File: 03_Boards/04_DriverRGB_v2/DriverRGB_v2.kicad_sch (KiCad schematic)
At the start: 22 parts, among them J1 PJ-102A, J2 S4B-ZR-SM4A, J3 20021121-00006C1LF, Q1 FDD8880, Q2 FDD8880, Q3 FDD8880, U1 ESP-12S, U3 AMS1117CD-3.3

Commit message: PCB
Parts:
- added R9: 10kOhm, Resistor_SMD:R_0603_1608Metric, symbol Device:R
- C3, C4: value 100nF -> 1nF
- S1: value Enable -> Reset
- S2: value IO0 -> Boot
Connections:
- net EN: now also R9.2, S1.2; no longer R9.1, S1.1
- net GND: now also S1.1; no longer R9.2
- net IO0: now also R9.2
- net VDD: now also R9.1, R9.1; no longer S1.2
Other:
- note added: "SWITCH BUTTON"
- moved on the sheet: C3, C4, J3, Q1, R2, R3, R9, S1, S2, U1

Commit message: Memoria
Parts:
- removed C4: 1nF, Capacitor_SMD:C_0603_1608Metric, symbol Device:C
- added R9 (x3): 10kOhm, Resistor_SMD:R_0603_1608Metric, symbol Device:R
- C3: value 1nF -> 100nF
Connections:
- net EN: no longer U1.3 (EN)
- net GND: now also R9.1
- net PWM_RED: now also U1.5 (IO14); no longer U1.4 (IO16)
- net VDD: now also R9.1, R9.2
- net RST: now reaches U1.1 (RST)
- net at U1.10 (IO15): now also R9.2
- net at U1.11 (IO2): now also R9.1
- new net: R9.2, U1.3 (EN)
- no-connect marks 8 -> 5

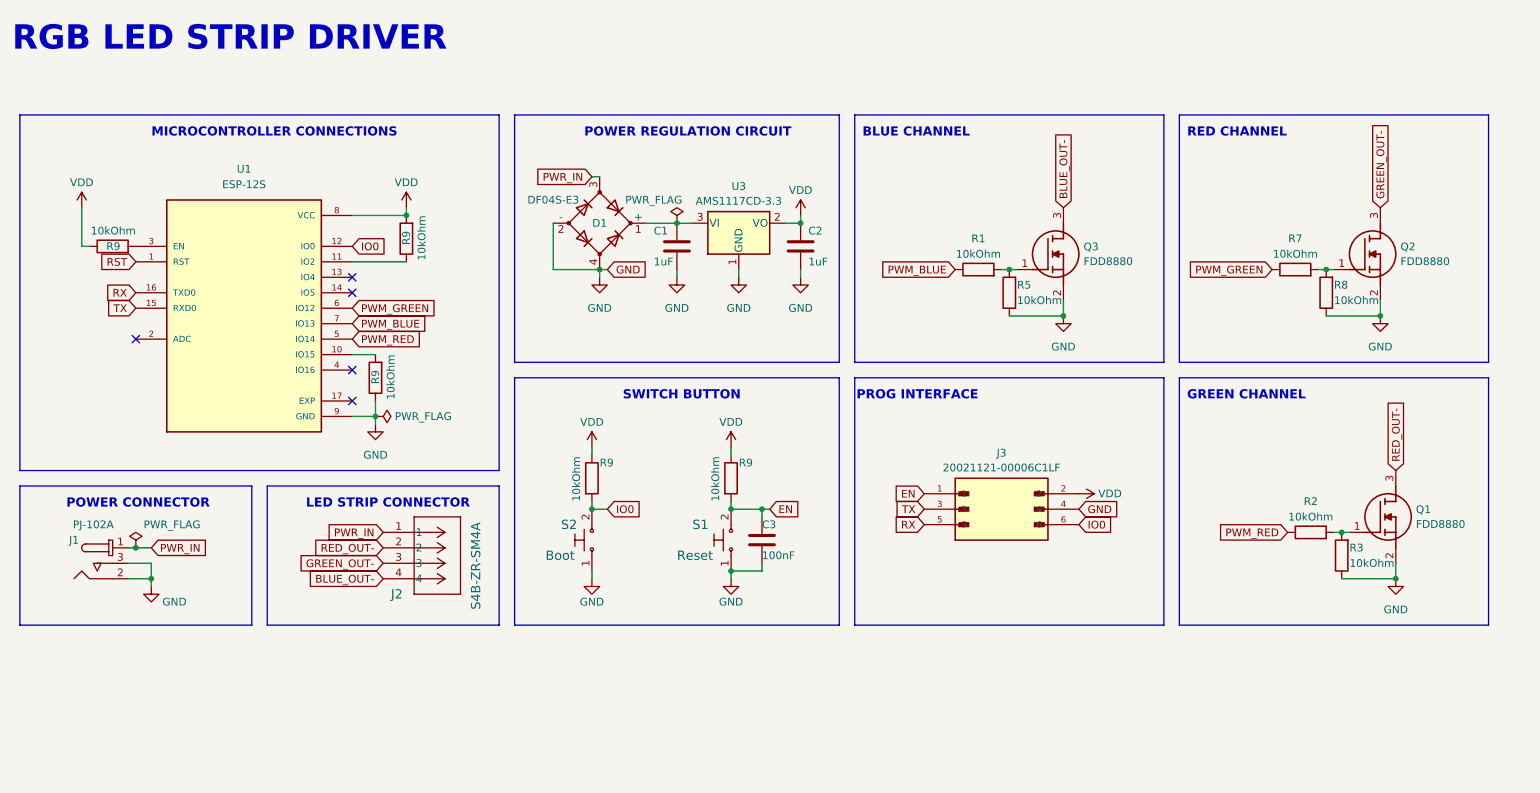
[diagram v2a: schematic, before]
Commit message: Rediseño del esquemático del PCB
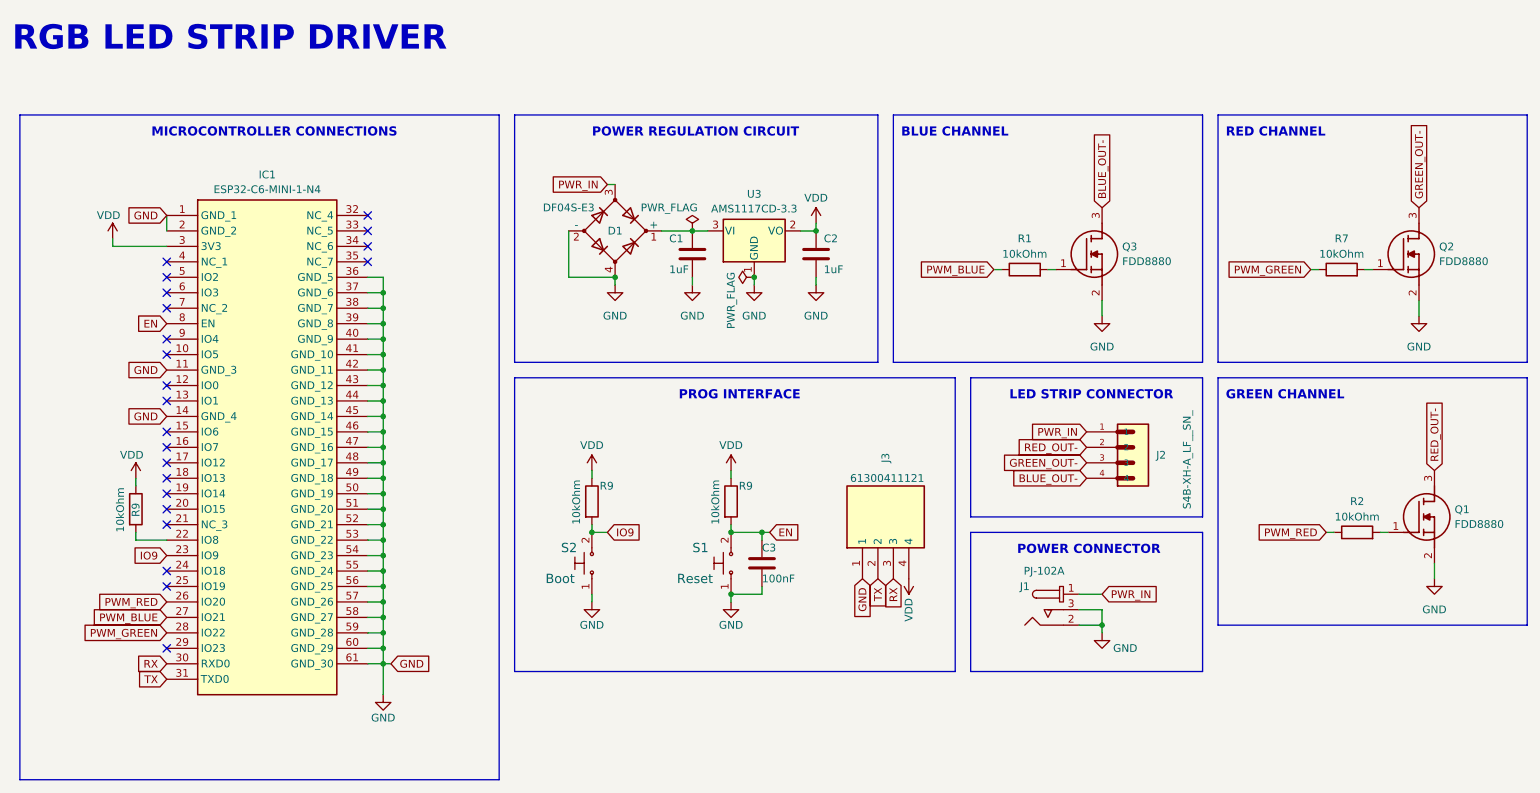
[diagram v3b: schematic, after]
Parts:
- removed J2: S4B-ZR-SM4A, 01_Footprints:S4B-ZR-SM4A-TF-LF, symbol S4B-ZR-SM4A-TF-LF:S4B-ZR-SM4A-TFLFSN
- removed J3: 20021121-00006C1LF, 01_Footprints:20021121-00006C1LF, symbol 20021121-00006C1LF:20021121-00006C1LF
- removed R3, R5, R8, R9 (x3): 10kOhm, Resistor_SMD:R_0603_1608Metric, symbol Device:R
- removed U1: ESP-12S, 01_Footprints:ESP-12S, symbol ESP-12S:ESP-12S
- added IC1: ESP32-C6-MINI-1-N4, 01_Footprints:ESP32-C6-MINI-1-N4, symbol ESP32-C6-MINI-1-N4:ESP32-C6-MINI-1-N4
- added J2: S4B-XH-A_LF__SN_, 01_Footprints:S4B-XH-A_LF__SN_, symbol S4B-XH-A_LF__SN_:S4B-XH-A_LF__SN_
- added J3: 61300411121, 01_Footprints:61300411121, symbol 61300411121:61300411121
- added R9: 10kOhm, Resistor_SMD:R_0603_1608Metric, symbol Device:R
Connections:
- net BLUE_OUT-: now also J2.4
- net EN: now also IC1.8 (EN)
- net GND: now also IC1.1 (GND_1), IC1.11 (GND_3), IC1.14 (GND_4), IC1.2 (GND_2), IC1.36 (GND_5), IC1.37 (GND_6), IC1.38 (GND_7), IC1.39 (GND_8), IC1.40 (GND_9), IC1.41 (GND_10), IC1.42 (GND_11), IC1.43 (GND_12), IC1.44 (GND_13), IC1.45 (GND_14), IC1.46 (GND_15), IC1.47 (GND_16), IC1.48 (GND_17), IC1.49 (GND_18), IC1.50 (GND_19), IC1.51 (GND_20), IC1.52 (GND_21), IC1.53 (GND_22), IC1.54 (GND_23), IC1.55 (GND_24), IC1.56 (GND_25), IC1.57 (GND_26), IC1.58 (GND_27), IC1.59 (GND_28), IC1.60 (GND_29), IC1.61 (GND_30), J3.1
- net GREEN_OUT-: now also J2.3
- net PWM_BLUE: now also IC1.27 (IO21)
- net PWM_GREEN: now also IC1.28 (IO22)
- net PWM_RED: now also IC1.26 (IO20)
- net PWR_IN: now also J2.1
- net RED_OUT-: now also J2.2
- net RX: now also IC1.30 (RXD0), J3.3
- net TX: now also IC1.31 (TXD0), J3.2
- net VDD: now also IC1.3 (3V3), J3.4, R9.1
- net IO0 renamed IO9
- net IO9: now also IC1.23 (IO9)
- new net: IC1.22 (IO8), R9.2
- no-connect marks 5 -> 22
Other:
- note removed: "SWITCH BUTTON"
- moved on the sheet: C1, C2, C3, D1, J1, Q1, Q2, Q3, R1, R2, R7, R9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

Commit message: Board desing v2
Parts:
- renumbered U3 to U1
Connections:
- net PWM_BLUE: now also IC1.26 (IO20); no longer IC1.27 (IO21)
- net PWM_GREEN: now also IC1.27 (IO21); no longer IC1.28 (IO22)
- net PWM_RED: now also IC1.28 (IO22); no longer IC1.26 (IO20)
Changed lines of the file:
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@@
   (title_block
     (title "RGB LED STRIP DRIVER")
-    (date "18/06/2024")
+    (date "20/06/2024")
     (rev "v02")
     (company "Schematic")
@@
     )
   )
-  (global_label "PWM_RED" (shape input) (at 52.07 128.27 180) (fields_autoplaced)
-    (effects (font (size 1.27 1.27)) (justify right))
-    (property "Intersheetrefs" "${INTERSHEET_REFS}" (at 40.2554 128.27 0)
+  (global_label "PWM_RED" (shape input) (at 52.07 133.35 180) (fields_autoplaced)
+    (effects (font (size 1.27 1.27)) (justify right))
+    (property "Intersheetrefs" "${INTERSHEET_REFS}" (at 40.2554 133.35 0)
       (effects (font (size 1.27 1.27)) (justify right) hide)
     )
@@
     )
   )
-  (global_label "PWM_GREEN" (shape input) (at 52.07 133.35 180) (fields_autoplaced)
-    (effects (font (size 1.27 1.27)) (justify right))
-    (property "Intersheetrefs" "${INTERSHEET_REFS}" (at 37.7759 133.35 0)
+  (global_label "PWM_GREEN" (shape input) (at 52.07 130.81 180) (fields_autoplaced)
+    (effects (font (size 1.27 1.27)) (justify right))
+    (property "Intersheetrefs" "${INTERSHEET_REFS}" (at 37.7759 130.81 0)
       (effects (font (size 1.27 1.27)) (justify right) hide)
     )
@@
     )
   )
-  (global_label "PWM_BLUE" (shape input) (at 52.07 130.81 180) (fields_autoplaced)
-    (effects (font (size 1.27 1.27)) (justify right))
-    (property "Intersheetrefs" "${INTERSHEET_REFS}" (at 39.1668 130.81 0)
+  (global_label "PWM_BLUE" (shape input) (at 52.07 128.27 180) (fields_autoplaced)
+    (effects (font (size 1.27 1.27)) (justify right))
+    (property "Intersheetrefs" "${INTERSHEET_REFS}" (at 39.1668 128.27 0)
       (effects (font (size 1.27 1.27)) (justify right) hide)
     )
@@
       (project "DriverRGB_v2"
         (path "/8cad6e61-0be6-474b-8ad7-614d0726c0fd"
-          (reference "C3") (unit 1)
+          (reference "C2") (unit 1)
         )
       )
@@
       (project "DriverRGB_v2"
         (path "/8cad6e61-0be6-474b-8ad7-614d0726c0fd"
-          (reference "C4") (unit 1)
+          (reference "C3") (unit 1)
         )
       )
@@
       (project "DriverRGB_v2"
         (path "/8cad6e61-0be6-474b-8ad7-614d0726c0fd"
-          (reference "R7") (unit 1)
+          (reference "R5") (unit 1)
         )
       )
@@
       (project "DriverRGB_v2"
         (path "/8cad6e61-0be6-474b-8ad7-614d0726c0fd"
-          (reference "R8") (unit 1)
+          (reference "R6") (unit 1)
         )
       )
@@
   (symbol (lib_id "Regulator_Linear:AMS1117CD-3.3") (at 148.59 67.31 0) (unit 1)
     (in_bom yes) (on_board yes) (dnp no) (fields_autoplaced)
-    (property "Reference" "U3" (at 148.59 61.2607 0)
+    (property "Reference" "U1" (at 148.59 61.2607 0)
       (effects (font (size 1.27 1.27)))
     )
@@
       (project "DriverRGB_v2"
         (path "/8cad6e61-0be6-474b-8ad7-614d0726c0fd"
-          (reference "U3") (unit 1)
+          (reference "U1") (unit 1)
         )
       )
@@
       (project "DriverRGB_v2"
         (path "/8cad6e61-0be6-474b-8ad7-614d0726c0fd"
-          (reference "R5") (unit 1)
-        )
-      )
+          (reference "R4") (unit 1)
+        )
+      )
